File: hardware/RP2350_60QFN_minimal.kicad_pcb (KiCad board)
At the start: 2 copper layers, 52 x 51 mm, 128 parts, among them J1 UJ20-C-H-G-SMT-2A-P16-TR, J1 USB_B_Micro, J2 73101-0570, J2 Conn_02x18_Odd_Even, J3 73101-0570, J3 Conn_02x18_Odd_Even, J4 SM03B-SRSS-TB, J5 4677, SW1 SW_Push, SW2 SW_Push, U1 RP2350_60QFN, U10 ADG621BRMZ, U13 TLP3441TP_F, U15 ADG621BRMZ, U2 NCP1117-3.3_SOT223, U2 REF35330QDBVR, U3 W25Q128JVS, U4 LM27762, U5 NCP1117-3.3_SOT223, U6 MCP47FEB02A0T-E/ST, U7 Opamp_Dual, U8 TLP3441TP_F, Y1 ABM8-272-T3

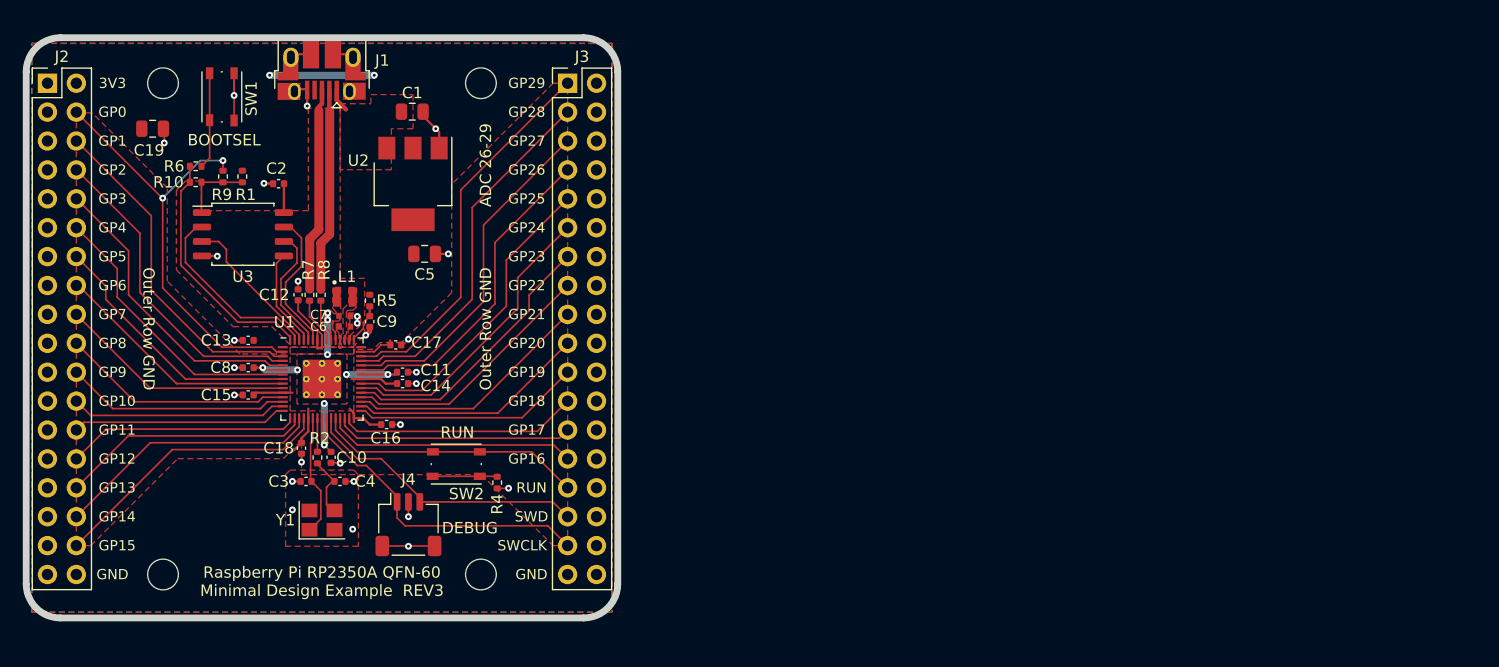
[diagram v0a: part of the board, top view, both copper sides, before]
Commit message: feat(hardware): Add test point connections + update PCB layout
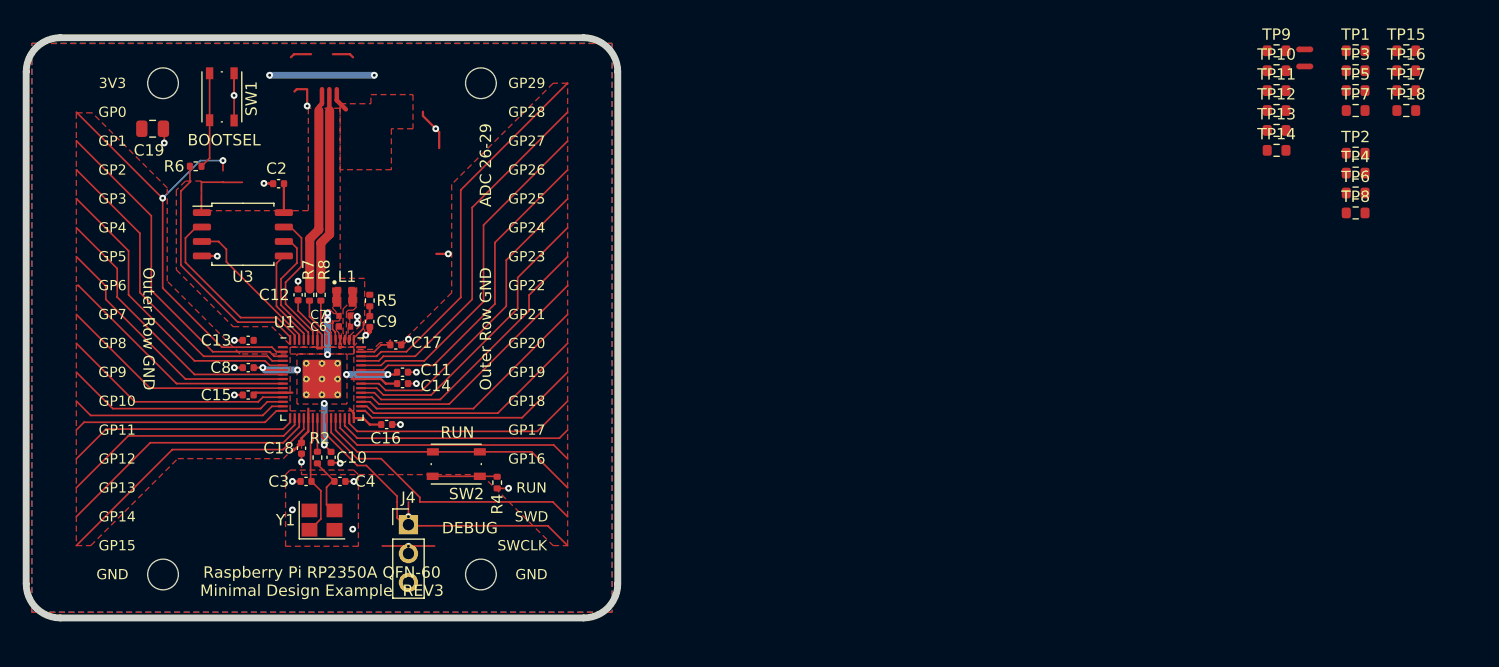
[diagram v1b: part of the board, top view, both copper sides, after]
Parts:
- removed the C1 at (107.9, 76.5)
- removed the C5 at (109.0, 89.0)
- removed the J1 at (100.0, 72.8)
- removed the J2 at (75.9, 74.0)
- removed the J3 at (121.6, 74.0)
- removed the R1 at (93.0, 82.2)
- removed the R10 at (88.9, 82.7)
- removed the R9 at (91.3, 82.2)
- removed the U2 at (108.0, 82.8)
- added NT1: NetTie_2, NetTie:NetTie-2_SMD_Pad0.5mm, F.Cu at (186.4, 71.0)
- added NT2: NetTie_2, NetTie:NetTie-2_SMD_Pad0.5mm, F.Cu at (186.4, 72.5)
- added TP1: TestPoint, CustomTestPoints:TestPoint_0603_1608Metric, F.Cu at (190.9, 71.2)
- added TP10: TestPoint, CustomTestPoints:TestPoint_0603_1608Metric, F.Cu at (183.9, 72.9)
- added TP11: TestPoint, CustomTestPoints:TestPoint_0603_1608Metric, F.Cu at (183.9, 74.7)
- added TP12: TestPoint, CustomTestPoints:TestPoint_0603_1608Metric, F.Cu at (183.9, 76.4)
- added TP13: TestPoint, CustomTestPoints:TestPoint_0603_1608Metric, F.Cu at (183.9, 78.2)
- added TP14: TestPoint, CustomTestPoints:TestPoint_0603_1608Metric, F.Cu at (183.9, 79.9)
- added TP15: TestPoint, CustomTestPoints:TestPoint_0603_1608Metric, F.Cu at (195.3, 71.2)
- added TP16: TestPoint, CustomTestPoints:TestPoint_0603_1608Metric, F.Cu at (195.3, 72.9)
- added TP17: TestPoint, CustomTestPoints:TestPoint_0603_1608Metric, F.Cu at (195.3, 74.7)
- added TP18: TestPoint, CustomTestPoints:TestPoint_0603_1608Metric, F.Cu at (195.3, 76.4)
- added TP2: TestPoint, CustomTestPoints:TestPoint_0603_1608Metric, F.Cu at (190.9, 80.2)
- added TP3: TestPoint, CustomTestPoints:TestPoint_0603_1608Metric, F.Cu at (190.9, 72.9)
- added TP4: TestPoint, CustomTestPoints:TestPoint_0603_1608Metric, F.Cu at (190.9, 81.9)
- added TP5: TestPoint, CustomTestPoints:TestPoint_0603_1608Metric, F.Cu at (190.9, 74.7)
- added TP6: TestPoint, CustomTestPoints:TestPoint_0603_1608Metric, F.Cu at (190.9, 83.7)
- added TP7: TestPoint, CustomTestPoints:TestPoint_0603_1608Metric, F.Cu at (190.9, 76.4)
- added TP8: TestPoint, CustomTestPoints:TestPoint_0603_1608Metric, F.Cu at (190.9, 85.4)
- added TP9: TestPoint, CustomTestPoints:TestPoint_0603_1608Metric, F.Cu at (183.9, 71.2)
- J4: value SM03B-SRSS-TB -> PinHeader_1x03; footprint Connector_JST:JST_SH_SM03B-SRSS-TB_1x03-1MP_P1.00mm_Horizontal -> Connector_PinHeader_2.54mm:PinHeader_1x03_P2.54mm_Vertical
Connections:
- C28 pad 1: +3V3 -> +3V3A
- U7 pad 4: GND -> GNDA
- U7 pad 8: +3V3 -> +3V3A
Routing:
- net unconnected-(U1-GPIO0-Pad2): track 0.00 -> 39.0 mm, vias 0 -> 2
- net /GPIO0: track 39.0 -> 0.00 mm, vias 2 -> 0
- net unconnected-(U1-GPIO29_ADC3-Pad43): track 0.00 -> 33.6 mm
- net /GPIO29_ADC3: track 33.6 -> 0.00 mm
- net unconnected-(U1-GPIO28_ADC2-Pad42): track 0.00 -> 31.9 mm
- net /GPIO28_ADC2: track 31.9 -> 0.00 mm
- net /GPIO27_ADC1: track 30.3 -> 0.00 mm
- net /CHB_ADC: track 0.00 -> 30.3 mm
- net unconnected-(U1-GPIO1-Pad3): track 0.00 -> 29.8 mm
- net /GPIO1: track 29.8 -> 0.00 mm
- net /GPIO26_ADC0: track 28.6 -> 0.00 mm
- net /CHA_ADC: track 0.00 -> 28.6 mm
- net /~{FLASH_CS}: track 0.00 -> 28.3 mm
- net unconnected-(U1-GPIO2-Pad4): track 0.00 -> 28.2 mm
- net /GPIO2: track 28.2 -> 0.00 mm
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
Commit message: feat(hardware): Update PCB layout for power and trigger blocks
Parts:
- U7: footprint Package_DIP:DIP-8_W7.62mm_Socket_LongPads -> MCP6572T_E_SN:SOIC127P600X175-8N
- moved C1 245.7 mm to (34.2, 34.7)
- moved C21 240.2 mm to (35.9, 49.0), turned to -90 degrees
- moved U5 237.0 mm to (34.1, 41.2), turned to -90 degrees
- moved J1 233.4 mm to (44.0, 18.2), turned to 180 degrees
- moved U2 232.4 mm to (41.4, 37.1), turned to -90 degrees
- moved R9 228.6 mm to (42.0, 28.4), turned to -90 degrees
- moved D6 228.1 mm to (62.1, 23.3)
- moved D7 226.9 mm to (61.0, 31.4)
- moved R1 224.6 mm to (45.5, 28.4), turned to -90 degrees
- moved C26 223.8 mm to (40.9, 33.9)
- moved U4 223.1 mm to (61.5, 27.2)
- moved C27 221.6 mm to (41.1, 40.8), turned to 90 degrees
- moved C37 221.2 mm to (42.4, 40.8), turned to -90 degrees
- moved R11 220.1 mm to (55.6, 24.6)
- moved R10 216.9 mm to (58.1, 24.6), turned to 180 degrees
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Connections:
- C23 pad 2: GNDA -> GND
- C24 pad 2: GNDA -> GND
- C25 pad 2: GNDA -> GND
- C5 pad 2: GNDA -> GND
- R11 pad 1: GNDA -> GND
- R13 pad 1: GNDA -> GND
- U4 pad 13: GNDA -> GND
- U4 pad 4: GNDA -> GND
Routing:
- net unconnected-(U1-GPIO0-Pad2): track 39.0 -> 0.00 mm, vias 2 -> 0
- net +3V3: track 37.6 -> 0.00 mm, vias 2 -> 0
- net GND: track 36.2 -> 0.00 mm, vias 26 -> 0
- net unconnected-(U1-GPIO29_ADC3-Pad43): track 33.6 -> 0.00 mm
- net unconnected-(U1-GPIO28_ADC2-Pad42): track 31.9 -> 0.00 mm
- net /CHB_ADC: track 30.3 -> 0.00 mm
- net unconnected-(U1-GPIO1-Pad3): track 29.8 -> 0.00 mm
- net /SWCLK: track 29.1 -> 0.00 mm, vias 1 -> 0
- net /CHA_ADC: track 28.6 -> 0.00 mm
- net /~{FLASH_CS}: track 28.3 -> 0.00 mm
- net unconnected-(U1-GPIO2-Pad4): track 28.2 -> 0.00 mm
- net unconnected-(U1-GPIO25-Pad37): track 27.7 -> 0.00 mm
- net unconnected-(U1-GPIO3-Pad5): track 26.5 -> 0.00 mm
- net unconnected-(U1-GPIO24-Pad36): track 26.1 -> 0.00 mm
- net /SWD: track 25.4 -> 0.00 mm
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- removed copper zone on F.Cu, net +1V1
- removed copper zone on F.Cu, net +3V3
- removed copper zone on F.Cu, net /VREG_LX
- removed copper zone on B.Cu, net GND
- removed copper zone on F.Cu, net GND
- removed copper zone on F.Cu, net VBUS
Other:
- board outline removed
- board text added: "Oscope REV1"
- board text removed: "3V3"
- board text removed: "ADC 26-29"
- board text removed: "GND"
- board text removed: "GP0"
- board text removed: "GP1"
- board text removed: "GP10"
- board text removed: "GP11"
- board text removed: "GP12"
- board text removed: "GP13"
- board text removed: "GP14"
- board text removed: "GP15"
- board text removed: "GP16"
- board text removed: "GP17"
- board text removed: "GP18"
- board text removed: "GP19"
- board text removed: "GP2"
- board text removed: "GP20"
- board text removed: "GP21"
- board text removed: "GP22"
- board text removed: "GP23"
- board text removed: "GP24"
- board text removed: "GP25"
- board text removed: "GP26"
- board text removed: "GP27"
- board text removed: "GP28"
- board text removed: "GP29"
- board text removed: "GP3"
- board text removed: "GP4"
- board text removed: "GP5"
- board text removed: "GP6"
- board text removed: "GP7"
- board text removed: "GP8"
- board text removed: "GP9"
- board text removed: "Minimal Design Example REV3"
- board text removed: "Outer Row GND"
- board text removed: "Raspberry Pi RP2350A QFN-60"
- board text removed: "SWCLK"
- board text removed: "SWD"

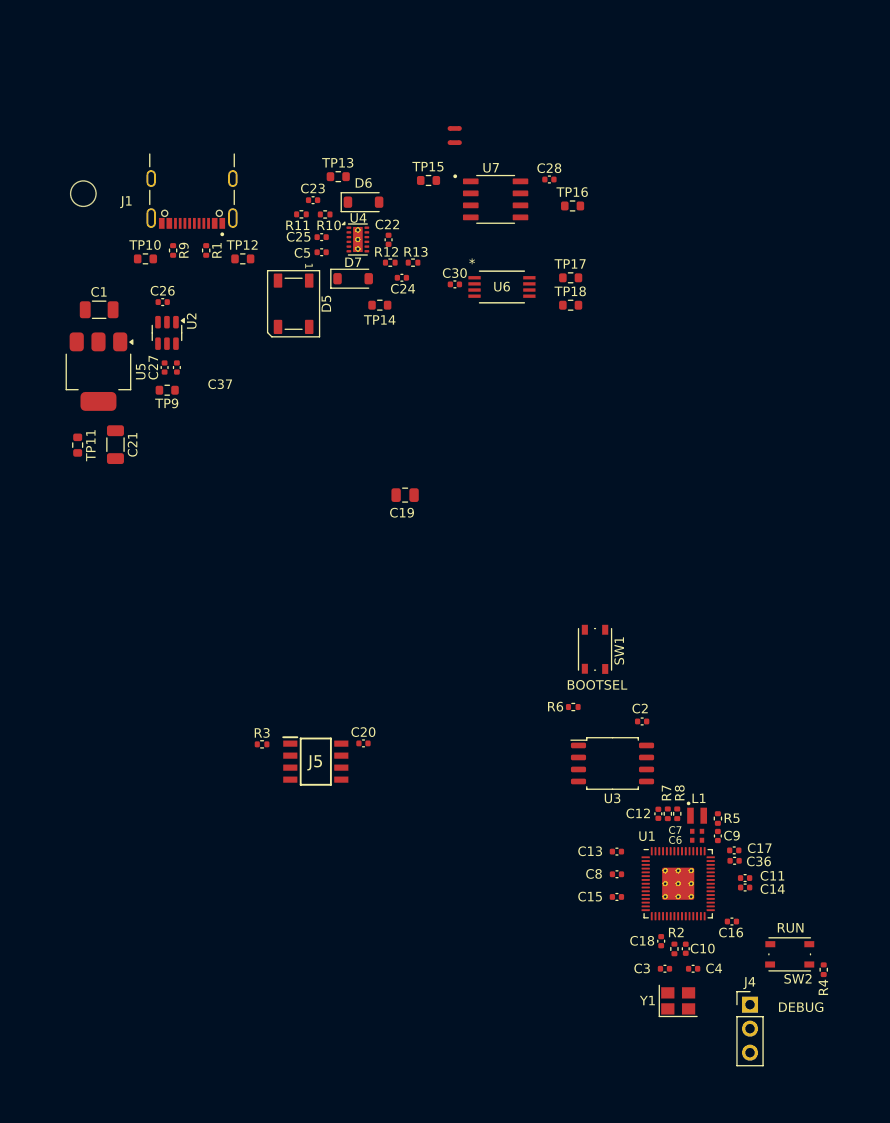
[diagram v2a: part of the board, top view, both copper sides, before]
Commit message: feat(hardware): Organize MCU block layout
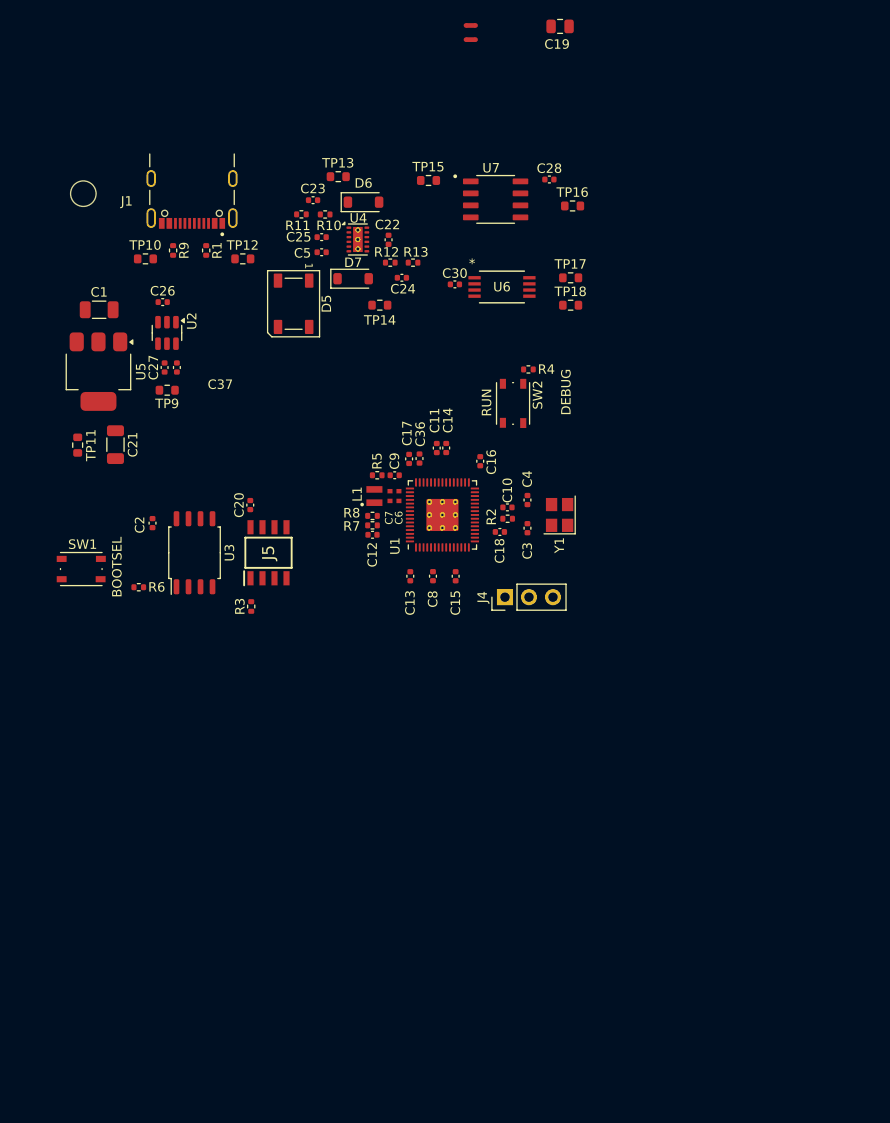
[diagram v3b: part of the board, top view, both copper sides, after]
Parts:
- moved R4 70.8 mm to (79.6, 41.0), turned to 0 degrees
- moved SW2 65.2 mm to (78.0, 44.6), turned to -90 degrees
- moved C14 56.2 mm to (70.9, 49.3), turned to 90 degrees
- moved C11 56.0 mm to (69.9, 49.3), turned to 90 degrees
- moved C2 55.9 mm to (39.8, 57.3), turned to -90 degrees
- moved C16 55.5 mm to (74.5, 50.7), turned to 90 degrees
- moved SW1 55.0 mm to (32.3, 62.1), turned to 0 degrees
- moved C36 54.1 mm to (68.1, 50.4), turned to 90 degrees
- moved C17 53.9 mm to (67.0, 50.5), turned to 90 degrees
- moved Y1 52.9 mm to (82.9, 56.4), turned to 90 degrees
- moved C4 52.6 mm to (79.5, 54.8), turned to 90 degrees
- moved C19 52.2 mm to (83.0, 4.70)
- moved C9 51.3 mm to (65.5, 52.2), turned to 0 degrees
- moved R5 51.2 mm to (63.6, 52.2), turned to 0 degrees
- moved C10 50.4 mm to (77.4, 55.6), turned to 0 degrees
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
